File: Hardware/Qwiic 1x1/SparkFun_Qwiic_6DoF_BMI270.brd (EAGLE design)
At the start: 25.4 x 25.4 mm, 64 parts, among them J1 QWIIC_RIGHT_ANGLE, J2 QWIIC_RIGHT_ANGLE, U1 BMI270

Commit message: Checklist updates
Change max VDD to VDD range
Add ordering instructions
Add axis labels to bottom silk
Add silk label to power LED
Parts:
- added U$33: (no value), SparkFun-Aesthetics:ORDERING_INSTRUCTIONS
- added U$34: (no value), output:PWR0
- added U$79: (no value), output:X0
- added U$80: (no value), output:Y0
- added U$81: (no value), output:Z0
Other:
- board text added: "Solder Mask: Red Thickness: 1.6mm Two layer design Finish: Lead Free HASL"
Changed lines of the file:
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@@
 <layer number="25" name="tNames" color="7" fill="1" visible="no" active="yes"/>
 <layer number="26" name="bNames" color="7" fill="1" visible="no" active="yes"/>
-<layer number="27" name="tValues" color="7" fill="1" visible="yes" active="yes"/>
+<layer number="27" name="tValues" color="7" fill="1" visible="no" active="yes"/>
 <layer number="28" name="bValues" color="7" fill="1" visible="no" active="yes"/>
 <layer number="29" name="tStop" color="7" fill="3" visible="no" active="yes"/>
@@
 </polygon>
 <wire x1="4.826" y1="17.78" x2="3.556" y2="16.51" width="0.254" layer="21" curve="-90"/>
+<text x="27.94" y="40.64" size="1.778" layer="51" font="vector" ratio="15" align="top-left">Solder Mask: Red
+Thickness: 1.6mm
+Two layer design
+Finish: Lead Free HASL</text>
+<circle x="3.556" y="16.51" radius="0.508" width="0.254" layer="22"/>
+<wire x1="1.397" y1="17.145" x2="1.397" y2="15.24" width="0.254" layer="22" style="shortdash"/>
+<wire x1="3.302" y1="18.923" x2="5.207" y2="18.923" width="0.254" layer="22" style="shortdash"/>
+<polygon width="0.254" layer="22">
+<vertex x="1.397" y="15.24"/>
+<vertex x="1.016" y="15.875"/>
+<vertex x="1.778" y="15.875"/>
+</polygon>
+<polygon width="0.254" layer="22">
+<vertex x="5.207" y="18.923"/>
+<vertex x="4.572" y="18.542"/>
+<vertex x="4.572" y="19.304"/>
+</polygon>
+<polygon width="0.254" layer="22">
+<vertex x="4.826" y="17.145"/>
+<vertex x="5.207" y="16.51"/>
+<vertex x="4.445" y="16.51"/>
+</polygon>
+<wire x1="0.762" y1="16.764" x2="2.032" y2="16.764" width="0.254" layer="22" curve="90"/>
+<wire x1="3.683" y1="18.288" x2="3.683" y2="19.558" width="0.254" layer="22" curve="90"/>
+<polygon width="0.254" layer="22">
+<vertex x="3.937" y="19.812"/>
+<vertex x="3.302" y="19.431"/>
+<vertex x="3.302" y="20.193"/>
+</polygon>
+<polygon width="0.254" layer="22">
+<vertex x="2.286" y="16.51"/>
+<vertex x="1.905" y="17.145"/>
+<vertex x="2.667" y="17.145"/>
+</polygon>
+<wire x1="3.556" y1="15.24" x2="4.826" y2="16.51" width="0.254" layer="22" curve="90"/>
+<wire x1="3.302" y1="16.256" x2="3.81" y2="16.764" width="0.254" layer="22"/>
+<wire x1="3.81" y1="16.256" x2="3.302" y2="16.764" width="0.254" layer="22"/>
 </plain>
 <attributes>
@@
 <element name="U$31" library="output" package="##OCS#_#0" value="" x="8.89" y="24.003" smashed="yes" rot="MR90"/>
 <element name="U$32" library="output" package="#OSDO_#0" value="" x="6.35" y="24.003" smashed="yes" rot="MR90"/>
+<element name="U$33" library="SparkFun-Aesthetics" package="ORDERING_INSTRUCTIONS" value="" x="26.67" y="50.8" smashed="yes"/>
+<element name="U$79" library="output" package="X0" value="" x="1.27" y="17.907" smashed="yes" rot="MR0"/>
+<element name="U$80" library="output" package="Y0" value="" x="2.54" y="19.05" smashed="yes" rot="MR0"/>
+<element name="U$81" library="output" package="Z0" value="" x="5.588" y="15.494" smashed="yes" rot="MR0"/>
+<element name="U$34" library="output" package="PWR0" value="" x="7.62" y="7.62" smashed="yes" rot="R90"/>
 </elements>
 <signals>
@@
 <wire x1="18.8214" y1="5.9436" x2="18.8214" y2="7.62" width="0.254" layer="16"/>
 </signal>
+<signal name="IMU_INT2">
+</signal>
 </signals>
 <mfgpreviewcolors>
@@
 </drawing>
 <compatibility>
+<note version="6.3" minversion="6.2.2" severity="warning">
+Since Version 6.2.2 text objects can contain more than one line,
+which will not be processed correctly with this version.
+</note>
 <note version="8.3" severity="warning">
 Since Version 8.3, EAGLE supports URNs for individual library

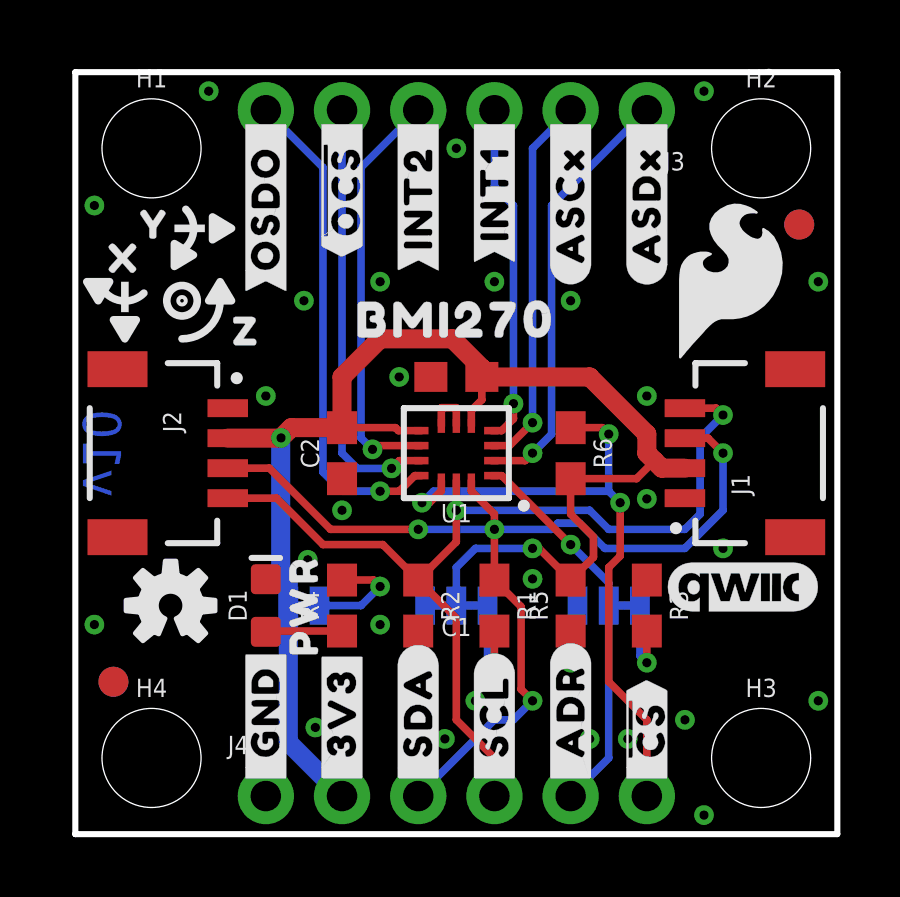
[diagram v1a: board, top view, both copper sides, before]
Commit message: Design review updates
Qwiic 1x1:
Add y position of headers to measures
Nudge I2C vias under right Qwiic connector
Nudge vias away from silk

Qwiic Micro:
Remove traces and vias under chip
Nudge via away from x-gyro arrowhead
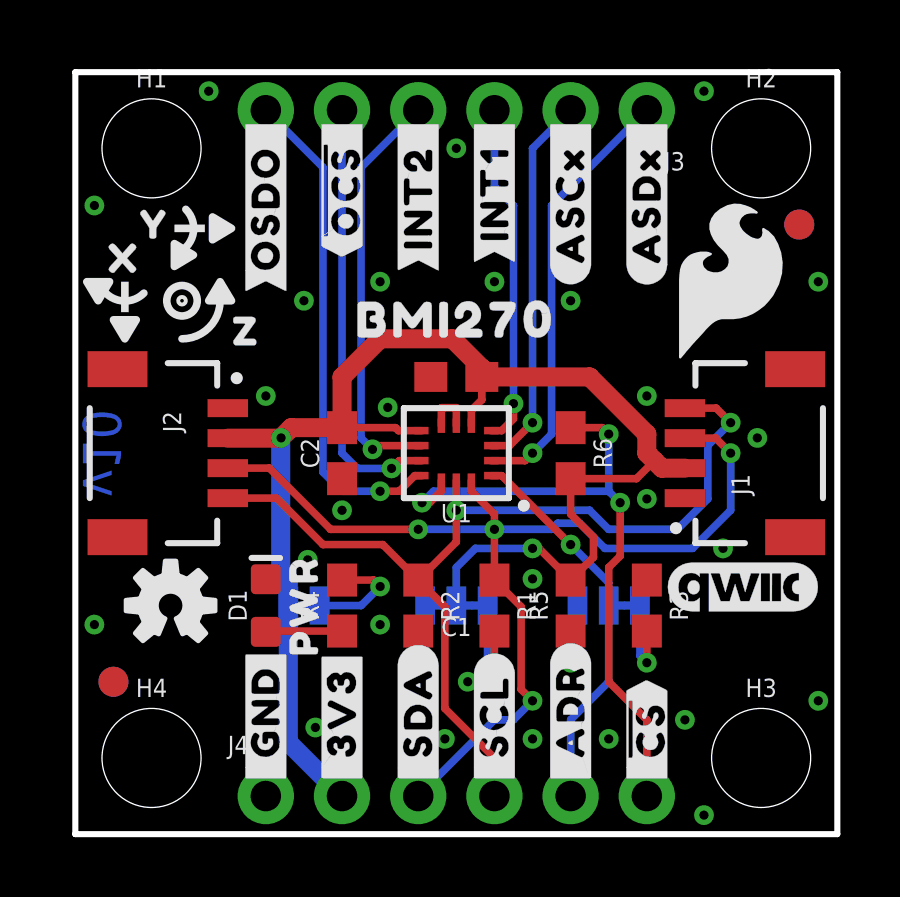
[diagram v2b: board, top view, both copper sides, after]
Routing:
- net SDA/PICO: track 35.0 -> 35.5 mm
- net GND: vias 27 -> 28
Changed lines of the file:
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@@
 <dimension x1="0" y1="0" x2="22.86" y2="0" x3="11.43" y3="-11.43" textsize="1.778" textratio="15" layer="47" unit="inch"/>
 <dimension x1="0" y1="0" x2="25.4" y2="0" x3="12.7" y3="-15.24" textsize="1.778" textratio="15" layer="47" unit="inch"/>
-<text x="-17.78" y="-2.54" size="1.778" layer="47" font="vector" ratio="15">Units: inches</text>
+<text x="-21.59" y="-2.54" size="1.778" layer="47" font="vector" ratio="15">Units: inches</text>
 <dimension x1="0" y1="0" x2="0" y2="2.54" x3="-1.27" y3="1.27" textsize="1.778" textratio="15" layer="47" unit="inch"/>
-<dimension x1="0" y1="0" x2="0" y2="12.7" x3="-5.08" y3="6.35" textsize="1.778" textratio="15" layer="47" unit="inch"/>
-<dimension x1="0" y1="0" x2="0" y2="22.86" x3="-8.89" y3="11.43" textsize="1.778" textratio="15" layer="47" unit="inch"/>
-<dimension x1="0" y1="0" x2="0" y2="25.4" x3="-12.7" y3="12.7" textsize="1.778" textratio="15" layer="47" unit="inch"/>
+<dimension x1="0" y1="0" x2="0" y2="12.7" x3="-8.89" y3="6.35" textsize="1.778" textratio="15" layer="47" unit="inch"/>
+<dimension x1="0" y1="0" x2="0" y2="22.86" x3="-12.7" y3="11.43" textsize="1.778" textratio="15" layer="47" unit="inch"/>
+<dimension x1="0" y1="0" x2="0" y2="25.4" x3="-20.32" y3="12.7" textsize="1.778" textratio="15" layer="47" unit="inch"/>
 <dimension x1="0" y1="25.4" x2="6.35" y2="25.4" x3="3.175" y3="26.67" textsize="1.778" textratio="15" layer="47" unit="inch"/>
 <dimension x1="0" y1="25.4" x2="19.05" y2="25.4" x3="9.525" y3="30.48" textsize="1.778" textratio="15" layer="47" unit="inch"/>
@@
 <wire x1="3.302" y1="16.256" x2="3.81" y2="16.764" width="0.254" layer="22"/>
 <wire x1="3.81" y1="16.256" x2="3.302" y2="16.764" width="0.254" layer="22"/>
+<dimension x1="0" y1="0" x2="0" y2="1.27" x3="-5.08" y3="0.635" textsize="1.778" textratio="15" layer="47" unit="inch"/>
+<dimension x1="0" y1="0" x2="0" y2="24.13" x3="-16.51" y3="12.065" textsize="1.778" textratio="15" layer="47" unit="inch"/>
+<rectangle x1="12.827" y1="5.969" x2="13.208" y2="6.223" layer="41"/>
 </plain>
 <attributes>
@@
 <via x="6.35" y="14.605" extent="1-16" drill="0.3048"/>
 <via x="19.05" y="11.176" extent="1-16" drill="0.3048"/>
-<via x="10.795" y="15.24" extent="1-16" drill="0.3048"/>
+<via x="10.414" y="14.224" extent="1-16" drill="0.3048"/>
 <wire x1="12.2" y1="14.216" x2="12.7" y2="14.216" width="0.254" layer="1"/>
 <via x="20.955" y="0.635" extent="1-16" drill="0.3048"/>
@@
 <via x="24.765" y="18.415" extent="1-16" drill="0.3048"/>
 <via x="20.955" y="24.765" extent="1-16" drill="0.3048"/>
-<via x="17.145" y="3.175" extent="1-16" drill="0.3048"/>
-<via x="18.415" y="3.175" extent="1-16" drill="0.3048"/>
-<via x="13.335" y="4.445" extent="1-16" drill="0.3048"/>
+<via x="15.24" y="3.175" extent="1-16" drill="0.3048"/>
+<via x="17.78" y="3.175" extent="1-16" drill="0.3048"/>
+<via x="13.081" y="5.08" extent="1-16" drill="0.3048"/>
 <via x="20.32" y="3.81" extent="1-16" drill="0.3048"/>
 <via x="10.16" y="18.415" extent="1-16" drill="0.3048"/>
@@
 <via x="19.05" y="14.605" extent="1-16" drill="0.3048"/>
 <via x="12.319" y="3.175" extent="1-16" drill="0.3048"/>
+<via x="22.733" y="13.208" extent="1-16" drill="0.3048"/>
 </signal>
 <signal name="ADR/POCI">
@@
 <contactref element="ADR" pad="2"/>
 <contactref element="J4" pad="5"/>
-<wire x1="16.51" y1="1.27" x2="17.78" y2="2.54" width="0.254" layer="16"/>
-<wire x1="17.78" y1="2.54" x2="17.78" y2="7.62" width="0.254" layer="16"/>
+<wire x1="17.78" y1="5.08" x2="16.51" y2="3.81" width="0.254" layer="16"/>
+<wire x1="16.51" y1="1.27" x2="16.51" y2="3.81" width="0.254" layer="16"/>
+<wire x1="17.78" y1="5.08" x2="17.78" y2="7.62" width="0.254" layer="16"/>
 <wire x1="17.78" y1="7.62" x2="17.78" y2="8.382" width="0.254" layer="16"/>
 <wire x1="17.78" y1="8.382" x2="16.51" y2="9.652" width="0.254" layer="16"/>
@@
 <wire x1="12.7" y1="9.74" x2="12.7" y2="10.795" width="0.254" layer="1"/>
 <wire x1="12.7" y1="10.795" x2="12.7" y2="11.7875" width="0.254" layer="1"/>
-<wire x1="11.43" y1="8.47" x2="12.7" y2="7.2" width="0.254" layer="1"/>
-<wire x1="12.7" y1="7.2" x2="12.7" y2="3.81" width="0.254" layer="1"/>
+<wire x1="11.43" y1="8.47" x2="12.319" y2="7.581" width="0.254" layer="1"/>
+<wire x1="12.319" y1="4.191" x2="12.319" y2="7.581" width="0.254" layer="1"/>
 <wire x1="13.97" y1="1.27" x2="13.97" y2="2.54" width="0.254" layer="1"/>
-<wire x1="13.97" y1="2.54" x2="12.7" y2="3.81" width="0.254" layer="1"/>
 <wire x1="5.08" y1="11.2" x2="6.707" y2="11.2" width="0.254" layer="1"/>
 <wire x1="6.707" y1="11.2" x2="8.255" y2="9.652" width="0.254" layer="1"/>
@@
 <wire x1="8.255" y1="9.652" x2="10.248" y2="9.652" width="0.254" layer="1"/>
 <wire x1="20.32" y1="14.2" x2="21.36" y2="14.2" width="0.254" layer="1"/>
-<wire x1="21.36" y1="14.2" x2="21.59" y2="13.97" width="0.254" layer="1"/>
-<via x="21.59" y="13.97" extent="1-16" drill="0.3048"/>
+<wire x1="21.36" y1="14.2" x2="21.844" y2="13.716" width="0.254" layer="1"/>
+<via x="21.844" y="13.716" extent="1-16" drill="0.3048"/>
 <via x="12.7" y="10.795" extent="1-16" drill="0.3048"/>
 <wire x1="12.7" y1="10.795" x2="17.145" y2="10.795" width="0.254" layer="16"/>
 <wire x1="17.145" y1="10.795" x2="17.78" y2="10.16" width="0.254" layer="16"/>
-<wire x1="17.78" y1="10.16" x2="20.32" y2="10.16" width="0.254" layer="16"/>
-<wire x1="20.32" y1="10.16" x2="20.828" y2="10.668" width="0.254" layer="16"/>
-<wire x1="20.828" y1="13.208" x2="21.59" y2="13.97" width="0.254" layer="16"/>
-<wire x1="20.828" y1="10.668" x2="20.828" y2="13.208" width="0.254" layer="16"/>
+<wire x1="17.78" y1="10.16" x2="20.066" y2="10.16" width="0.254" layer="16"/>
+<wire x1="20.066" y1="10.16" x2="21.082" y2="11.176" width="0.254" layer="16"/>
+<wire x1="21.082" y1="12.954" x2="21.844" y2="13.716" width="0.254" layer="16"/>
+<wire x1="21.082" y1="11.176" x2="21.082" y2="12.954" width="0.254" layer="16"/>
+<wire x1="13.97" y1="2.54" x2="12.319" y2="4.191" width="0.254" layer="1"/>
 </signal>
 <signal name="SDA/PICO">
@@
 <wire x1="13.2" y1="11.438" x2="13.2" y2="11.7875" width="0.254" layer="1"/>
 <wire x1="13.97" y1="8.47" x2="13.97" y2="10.16" width="0.254" layer="1"/>
-<wire x1="20.32" y1="13.2" x2="21.09" y2="13.2" width="0.254" layer="1"/>
-<wire x1="21.09" y1="13.2" x2="21.59" y2="12.7" width="0.254" layer="1"/>
-<via x="21.59" y="12.7" extent="1-16" drill="0.3048"/>
+<wire x1="20.32" y1="13.2" x2="21.344" y2="13.2" width="0.254" layer="1"/>
+<wire x1="21.344" y1="13.2" x2="21.844" y2="12.7" width="0.254" layer="1"/>
+<via x="21.844" y="12.7" extent="1-16" drill="0.3048"/>
 <wire x1="15.875" y1="10.16" x2="13.97" y2="10.16" width="0.254" layer="16"/>
-<wire x1="21.59" y1="12.7" x2="21.59" y2="10.795" width="0.254" layer="16"/>
-<wire x1="21.59" y1="10.795" x2="20.32" y2="9.525" width="0.254" layer="16"/>
-<wire x1="20.32" y1="9.525" x2="17.653" y2="9.525" width="0.254" layer="16"/>
+<wire x1="21.844" y1="12.7" x2="21.844" y2="10.795" width="0.254" layer="16"/>
+<wire x1="21.844" y1="10.795" x2="20.574" y2="9.525" width="0.254" layer="16"/>
+<wire x1="20.574" y1="9.525" x2="17.653" y2="9.525" width="0.254" layer="16"/>
 <wire x1="16.0782" y1="10.3632" x2="15.875" y2="10.16" width="0.254" layer="16"/>
 <wire x1="17.653" y1="9.525" x2="16.8148" y2="10.3632" width="0.254" layer="16"/>

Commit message: Design review updates
Add gap to linear axis silk to clarify gyro directions
Add GND via to Qwiic Micro
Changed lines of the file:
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@@
 <circle x="3.556" y="17.78" radius="0.0635" width="0.254" layer="21"/>
 <circle x="3.556" y="17.78" radius="0.508" width="0.254" layer="21"/>
-<wire x1="1.651" y1="18.415" x2="1.651" y2="16.51" width="0.254" layer="21" style="shortdash"/>
-<wire x1="3.302" y1="20.193" x2="5.207" y2="20.193" width="0.254" layer="21" style="shortdash"/>
 <polygon width="0.254" layer="21">
 <vertex x="1.651" y="16.51"/>
@@
 Finish: Lead Free HASL</text>
 <circle x="3.556" y="16.51" radius="0.508" width="0.254" layer="22"/>
-<wire x1="1.397" y1="17.145" x2="1.397" y2="15.24" width="0.254" layer="22" style="shortdash"/>
-<wire x1="3.302" y1="18.923" x2="5.207" y2="18.923" width="0.254" layer="22" style="shortdash"/>
 <polygon width="0.254" layer="22">
 <vertex x="1.397" y="15.24"/>
@@
 <dimension x1="0" y1="0" x2="0" y2="24.13" x3="-16.51" y3="12.065" textsize="1.778" textratio="15" layer="47" unit="inch"/>
 <rectangle x1="12.827" y1="5.969" x2="13.208" y2="6.223" layer="41"/>
+<wire x1="4.318" y1="20.193" x2="5.207" y2="20.193" width="0.254" layer="21" style="shortdash"/>
+<wire x1="3.302" y1="20.193" x2="3.556" y2="20.193" width="0.254" layer="21" style="shortdash"/>
+<wire x1="1.651" y1="17.399" x2="1.651" y2="16.51" width="0.254" layer="21" style="shortdash"/>
+<wire x1="1.651" y1="18.415" x2="1.651" y2="18.161" width="0.254" layer="21" style="shortdash"/>
+<wire x1="4.318" y1="18.923" x2="5.207" y2="18.923" width="0.254" layer="22" style="shortdash"/>
+<wire x1="3.302" y1="18.923" x2="3.556" y2="18.923" width="0.254" layer="22" style="shortdash"/>
+<wire x1="1.397" y1="16.129" x2="1.397" y2="15.24" width="0.254" layer="22" style="shortdash"/>
+<wire x1="1.397" y1="17.145" x2="1.397" y2="16.891" width="0.254" layer="22" style="shortdash"/>
 </plain>
 <attributes>

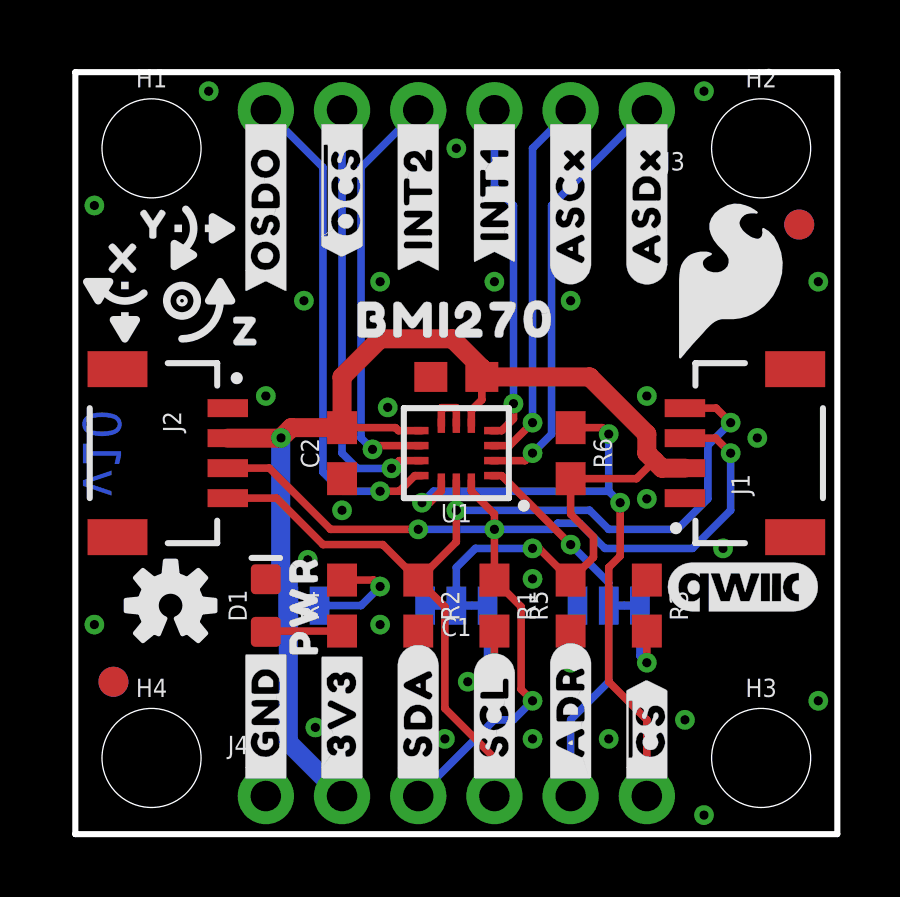
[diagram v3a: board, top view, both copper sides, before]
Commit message: Silk tweaks
Add silk lines between passive components
Nudge "BMI270" silk on Qwiic Micro
Add bigger pin 1 indicator dot to Qwiic Micro
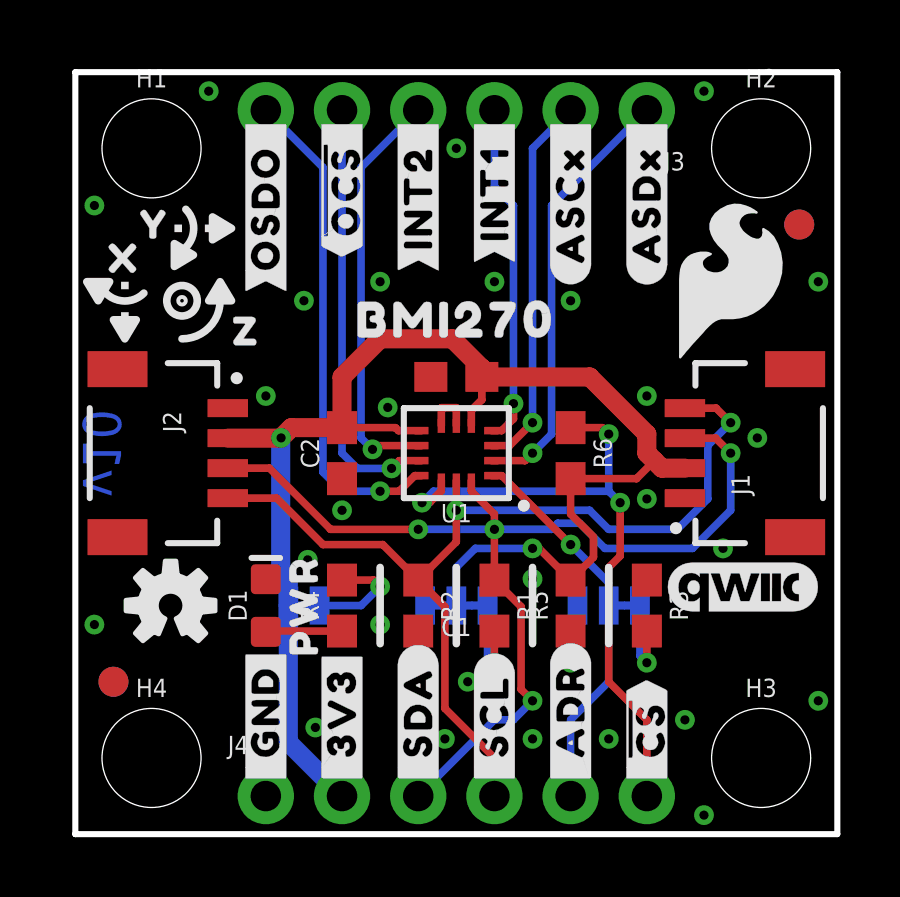
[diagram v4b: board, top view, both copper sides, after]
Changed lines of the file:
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@@
 <wire x1="1.397" y1="16.129" x2="1.397" y2="15.24" width="0.254" layer="22" style="shortdash"/>
 <wire x1="1.397" y1="17.145" x2="1.397" y2="16.891" width="0.254" layer="22" style="shortdash"/>
+<wire x1="12.7" y1="6.35" x2="12.7" y2="8.89" width="0.254" layer="21"/>
+<wire x1="15.24" y1="6.35" x2="15.24" y2="8.89" width="0.254" layer="21"/>
+<wire x1="17.78" y1="6.35" x2="17.78" y2="8.89" width="0.254" layer="21"/>
+<wire x1="10.16" y1="6.35" x2="10.16" y2="8.89" width="0.254" layer="21"/>
 </plain>
 <attributes>
